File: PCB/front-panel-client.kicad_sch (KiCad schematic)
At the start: 7 parts, among them IC16 PMV20ENR, IC18 PMV20ENR, J10 67996-408HLF

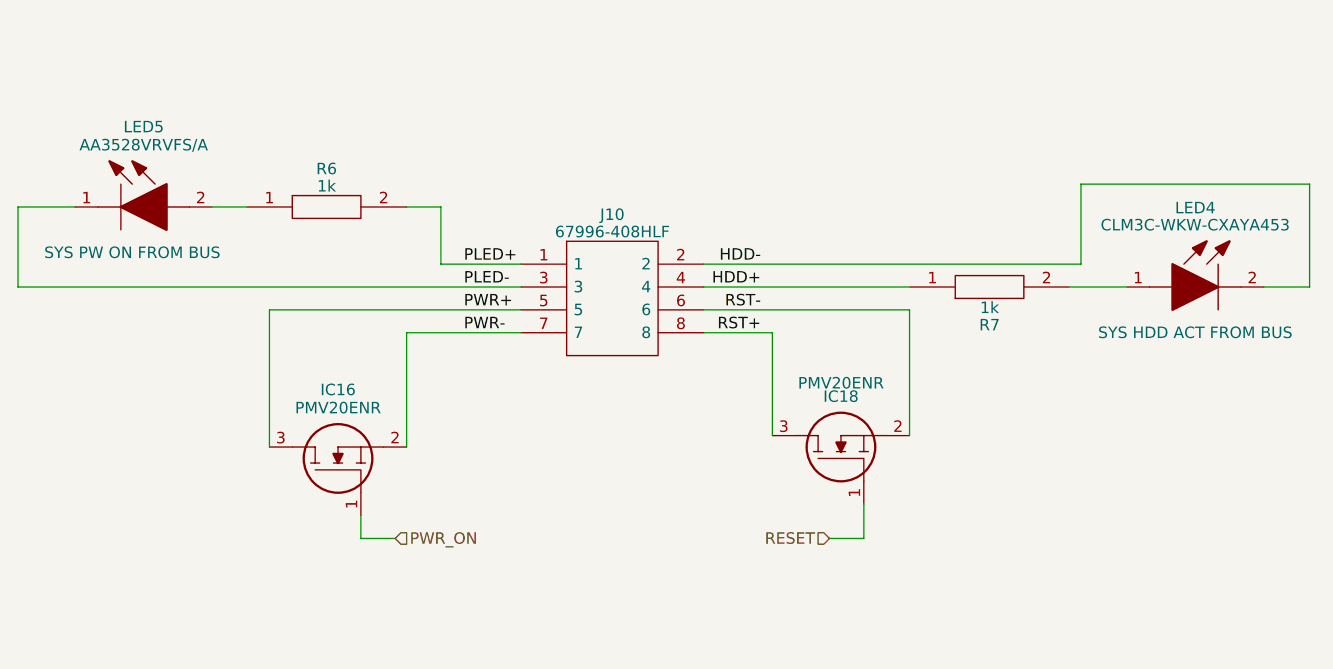
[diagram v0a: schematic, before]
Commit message: add pullup/down resistors and fix oro 6p lines with boot1/0
closes #24
closes #21
closes #15
closes #12
closes #6
closes #3
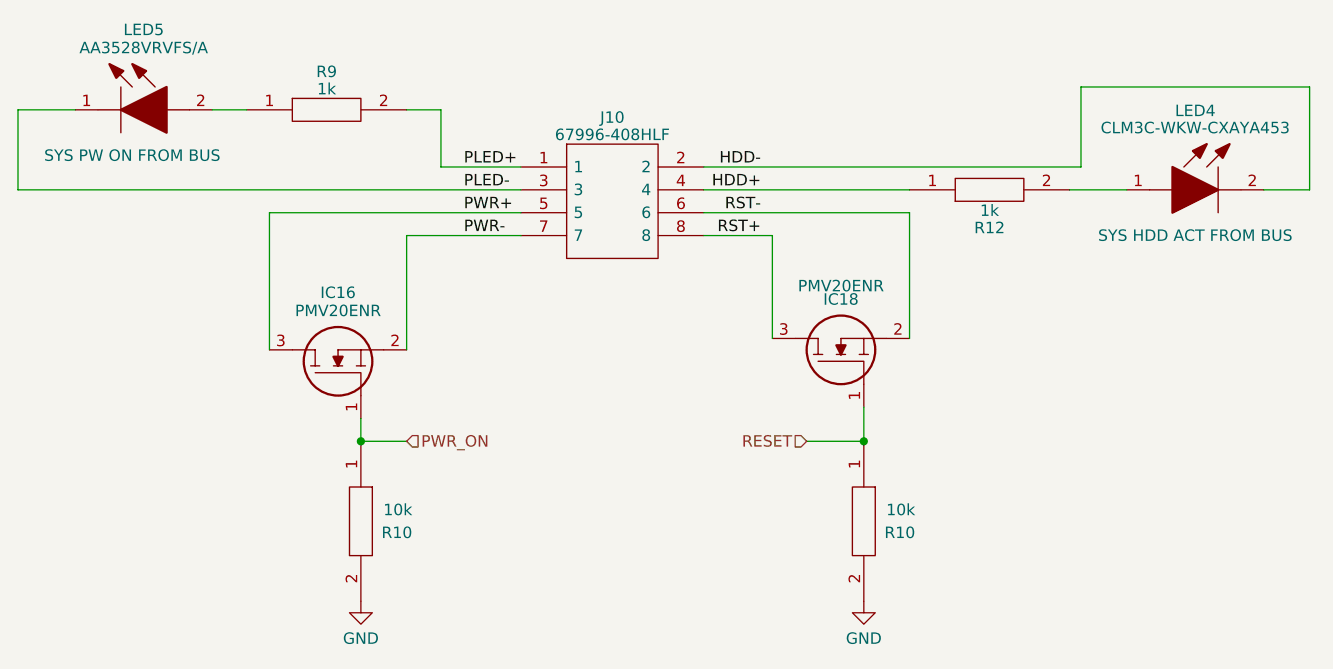
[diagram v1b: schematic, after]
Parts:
- added R10 (x2): 10k, SamacSys_Parts:RESC5025X65N, symbol SamacSys_Parts:RC2010JK-0710KL
- renumbered R7 to R12, R6 to R9
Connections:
- net PWR_ON: now also R10.1
- net RESET: now also R10.1
- new net GND: R10.2, R10.2
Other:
- moved on the sheet: IC16, IC18, J10, LED4, LED5, R12, R9

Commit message: switch 10k and 4.7k resistors to smaller packages (closes #32)
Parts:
- R10: footprint SamacSys_Parts:RESC5025X65N -> RESC5025X65N
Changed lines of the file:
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@@
       (effects (font (size 1.27 1.27)) (justify right))
     )
-    (property "Footprint" "SamacSys_Parts:RESC5025X65N" (at 173.99 134.62 0)
+    (property "Footprint" "RESC5025X65N" (at 173.99 134.62 0)
       (effects (font (size 1.27 1.27)) (justify left) hide)
     )
@@
       (effects (font (size 1.27 1.27)) (justify right))
     )
-    (property "Footprint" "SamacSys_Parts:RESC5025X65N" (at 118.11 134.62 0)
-      (effects (font (size 1.27 1.27)) (justify left) hide)
-    )
+    (property "Footprint" "RESC5025X65N" (at 118.11 134.62 0)
+      (effects (font (size 1.27 1.27)) (justify left) hide)
+    )

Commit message: actually reduce 10k package size (ref #32)
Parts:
- R10: footprint RESC5025X65N -> RESC1005X40N; symbol SamacSys_Parts:RC2010JK-0710KL -> SamacSys_Parts:RK73H1ETTP1002F; Arrow Part Number RC2010JK-0710KL -> RK73H1ETTP1002F; Arrow Price/Stock https://www.arrow.com/en/products/rc2010jk-0710kl/yageo -> https://www.arrow.com/en/products/rk73h1ettp1002f/koa-speer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; Height 0.65 -> 0.4; Manufacturer_Name KEMET -> KOA Speer; Manufacturer_Part_Number RC2010JK-0710KL -> RK73H1ETTP1002F; Mouser Part Number 603-RC2010JK-0710KL -> 660-RK73H1ETTP1002F; Mouser Price/Stock https://www.mouser.co.uk/ProductDetail/YAGEO/RC2010JK-0710K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 -> https://www.mouser.co.uk/ProductDetail/KOA-Speer/RK73H1ETTP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
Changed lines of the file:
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@@
     )
   )
-  (symbol (lib_id "SamacSys_Parts:RC2010JK-0710KL") (at 172.72 120.65 270) (unit 1)
+  (symbol (lib_id "SamacSys_Parts:RK73H1ETTP1002F") (at 172.72 120.65 270) (unit 1)
     (in_bom yes) (on_board yes) (dnp no)
     (property "Reference" "R10" (at 178.435 130.81 90)
@@
       (effects (font (size 1.27 1.27)) (justify right))
     )
-    (property "Footprint" "RESC5025X65N" (at 173.99 134.62 0)
-      (effects (font (size 1.27 1.27)) (justify left) hide)
-    )
-    (property "Datasheet" "https://www.arrow.com/en/products/rc2010jk-0710kl/yageo" (at 171.45 134.62 0)
-      (effects (font (size 1.27 1.27)) (justify left) hide)
-    )
-    (property "Description" "Res Thick Film 2010 10K Ohm 5% 0.75W(3/4W) +/-100ppm/C Pad SMD T/R" (at 168.91 134.62 0)
-      (effects (font (size 1.27 1.27)) (justify left) hide)
-    )
-    (property "Height" "0.65" (at 166.37 134.62 0)
-      (effects (font (size 1.27 1.27)) (justify left) hide)
-    )
-    (property "Manufacturer_Name" "KEMET" (at 163.83 134.62 0)
-      (effects (font (size 1.27 1.27)) (justify left) hide)
-    )
-    (property "Manufacturer_Part_Number" "RC2010JK-0710KL" (at 161.29 134.62 0)
-      (effects (font (size 1.27 1.27)) (justify left) hide)
-    )
-    (property "Mouser Part Number" "603-RC2010JK-0710KL" (at 158.75 134.62 0)
-      (effects (font (size 1.27 1.27)) (justify left) hide)
-    )
-    (property "Mouser Price/Stock" "https://www.mouser.co.uk/ProductDetail/YAGEO/RC2010JK-0710KL?qs=sNpmnPgvziOLj5uuquGIow%3D%3D" (at 156.21 134.62 0)
-      (effects (font (size 1.27 1.27)) (justify left) hide)
-    )
-    (property "Arrow Part Number" "RC2010JK-0710KL" (at 153.67 134.62 0)
-      (effects (font (size 1.27 1.27)) (justify left) hide)
-    )
-    (property "Arrow Price/Stock" "https://www.arrow.com/en/products/rc2010jk-0710kl/yageo" (at 151.13 134.62 0)
+    (property "Footprint" "RESC1005X40N" (at 173.99 134.62 0)
+      (effects (font (size 1.27 1.27)) (justify left) hide)
+    )
+    (property "Datasheet" "http://www.koaspeer.com/catimages/Products/RK73-RT/RK73-RT.pdf" (at 171.45 134.62 0)
+      (effects (font (size 1.27 1.27)) (justify left) hide)
+    )
+    (property "Description" "Resistor,ThickFilm1005,0.063W,10kohm" (at 168.91 134.62 0)
+      (effects (font (size 1.27 1.27)) (justify left) hide)
+    )
+    (property "Height" "0.4" (at 166.37 134.62 0)
+      (effects (font (size 1.27 1.27)) (justify left) hide)
+    )
+    (property "Manufacturer_Name" "KOA Speer" (at 163.83 134.62 0)
+      (effects (font (size 1.27 1.27)) (justify left) hide)
+    )
+    (property "Manufacturer_Part_Number" "RK73H1ETTP1002F" (at 161.29 134.62 0)
+      (effects (font (size 1.27 1.27)) (justify left) hide)
+    )
+    (property "Mouser Part Number" "660-RK73H1ETTP1002F" (at 158.75 134.62 0)
+      (effects (font (size 1.27 1.27)) (justify left) hide)
+    )
+    (property "Mouser Price/Stock" "https://www.mouser.co.uk/ProductDetail/KOA-Speer/RK73H1ETTP1002F?qs=uLfVlVfCHH2OZ4JTybrBPQ%3D%3D" (at 156.21 134.62 0)
+      (effects (font (size 1.27 1.27)) (justify left) hide)
+    )
+    (property "Arrow Part Number" "RK73H1ETTP1002F" (at 153.67 134.62 0)
+      (effects (font (size 1.27 1.27)) (justify left) hide)
+    )
+    (property "Arrow Price/Stock" "https://www.arrow.com/en/products/rk73h1ettp1002f/koa-speer-electronics?region=nac" (at 151.13 134.62 0)
       (effects (font (size 1.27 1.27)) (justify left) hide)
     )
@@
     )
   )
-  (symbol (lib_id "SamacSys_Parts:RC2010JK-0710KL") (at 116.84 120.65 270) (unit 1)
+  (symbol (lib_id "SamacSys_Parts:RK73H1ETTP1002F") (at 116.84 120.65 270) (unit 1)
     (in_bom yes) (on_board yes) (dnp no)
     (property "Reference" "R10" (at 122.555 130.81 90)
@@
       (effects (font (size 1.27 1.27)) (justify right))
     )
-    (property "Footprint" "RESC5025X65N" (at 118.11 134.62 0)
-      (effects (font (size 1.27 1.27)) (justify left) hide)
-    )
-    (property "Datasheet" "https://www.arrow.com/en/products/rc2010jk-0710kl/yageo" (at 115.57 134.62 0)
-      (effects (font (size 1.27 1.27)) (justify left) hide)
-    )
-    (property "Description" "Res Thick Film 2010 10K Ohm 5% 0.75W(3/4W) +/-100ppm/C Pad SMD T/R" (at 113.03 134.62 0)
-      (effects (font (size 1.27 1.27)) (justify left) hide)
-    )
-    (property "Height" "0.65" (at 110.49 134.62 0)
-      (effects (font (size 1.27 1.27)) (justify left) hide)
-    )
-    (property "Manufacturer_Name" "KEMET" (at 107.95 134.62 0)
-      (effects (font (size 1.27 1.27)) (justify left) hide)
-    )
-    (property "Manufacturer_Part_Number" "RC2010JK-0710KL" (at 105.41 134.62 0)
-      (effects (font (size 1.27 1.27)) (justify left) hide)
-    )
-    (property "Mouser Part Number" "603-RC2010JK-0710KL" (at 102.87 134.62 0)
-      (effects (font (size 1.27 1.27)) (justify left) hide)
-    )
-    (property "Mouser Price/Stock" "https://www.mouser.co.uk/ProductDetail/YAGEO/RC2010JK-0710KL?qs=sNpmnPgvziOLj5uuquGIow%3D%3D" (at 100.33 134.62 0)
-      (effects (font (size 1.27 1.27)) (justify left) hide)
-    )
-    (property "Arrow Part Number" "RC2010JK-0710KL" (at 97.79 134.62 0)
-      (effects (font (size 1.27 1.27)) (justify left) hide)
-    )
-    (property "Arrow Price/Stock" "https://www.arrow.com/en/products/rc2010jk-0710kl/yageo" (at 95.25 134.62 0)
-      (effects (font (size 1.27 1.27)) (justify left) hide)
-    )
+    (property "Footprint" "RESC1005X40N" (at 118.11 134.62 0)
+      (effects (font (size 1.27 1.27)) (justify left) hide)
+    )
+    (property "Datasheet" "http://www.koaspeer.com/catimages/Products/RK73-RT/RK73-RT.pdf" (at 115.57 134.62 0)
+      (effects (font (size 1.27 1.27)) (justify left) hide)
+    )
+    (property "Description" "Resistor,ThickFilm1005,0.063W,10kohm" (at 113.03 134.62 0)
+      (effects (font (size 1.27 1.27)) (justify left) hide)
+    )
+    (property "Height" "0.4" (at 110.49 134.62 0)
+      (effects (font (size 1.27 1.27)) (justify left) hide)
+    )
+    (property "Manufacturer_Name" "KOA Speer" (at 107.95 134.62 0)
+      (effects (font (size 1.27 1.27)) (justify left) hide)
+    )
+    (property "Manufacturer_Part_Number" "RK73H1ETTP1002F" (at 105.41 134.62 0)
+      (effects (font (size 1.27 1.27)) (justify left) hide)
+    )
+    (property "Mouser Part Number" "660-RK73H1ETTP1002F" (at 102.87 134.62 0)
+      (effects (font (size 1.27 1.27)) (justify left) hide)
+    )
+    (property "Mouser Price/Stock" "https://www.mouser.co.uk/ProductDetail/KOA-Speer/RK73H1ETTP1002F?qs=uLfVlVfCHH2OZ4JTybrBPQ%3D%3D" (at 100.33 134.62 0)
+      (effects (font (size 1.27 1.27)) (justify left) hide)
+    )
+    (property "Arrow Part Number" "RK73H1ETTP1002F" (at 97.79 134.62 0)
+      (effects (font (size 1.27 1.27)) (justify left) hide)
+    )
+    (property "Arrow Price/Stock" "https://www.arrow.com/en/products/rk73h1ettp1002f/koa-speer-electronics?region=nac" (at 95.25 134.62 0)
+      (effects (font (size 1.27 1.27)) (justify left) hide)
+    )

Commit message: re-annotate schematic
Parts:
- renumbered R9 to R10, R12 to R13
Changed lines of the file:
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@@
   (symbol (lib_id "SamacSys_Parts:SG73P2ATTD102J") (at 177.8 92.71 0) (mirror x) (unit 1)
     (in_bom yes) (on_board yes) (dnp no) (fields_autoplaced)
-    (property "Reference" "R12" (at 186.69 96.9391 0)
+    (property "Reference" "R13" (at 186.69 96.9391 0)
       (effects (font (size 1.27 1.27)))
     )
@@
       (project "OroLink"
         (path "/e89dcd22-1250-4a5b-b778-1c95a0dd623d/6eeb4496-d532-42b5-95b8-3d397c9a21d1"
-          (reference "R12") (unit 1)
+          (reference "R13") (unit 1)
         )
       )
@@
         )
         (path "/e89dcd22-1250-4a5b-b778-1c95a0dd623d/6eeb4496-d532-42b5-95b8-3d397c9a21d1"
-          (reference "R11") (unit 1)
+          (reference "R12") (unit 1)
         )
       )
@@
         )
         (path "/e89dcd22-1250-4a5b-b778-1c95a0dd623d/6eeb4496-d532-42b5-95b8-3d397c9a21d1"
-          (reference "R10") (unit 1)
+          (reference "R11") (unit 1)
         )
       )
@@
   (symbol (lib_id "SamacSys_Parts:SG73P2ATTD102J") (at 104.14 83.82 0) (unit 1)
     (in_bom yes) (on_board yes) (dnp no) (fields_autoplaced)
-    (property "Reference" "R9" (at 113.03 79.5909 0)
+    (property "Reference" "R10" (at 113.03 79.5909 0)
       (effects (font (size 1.27 1.27)))
     )
@@
       (project "OroLink"
         (path "/e89dcd22-1250-4a5b-b778-1c95a0dd623d/6eeb4496-d532-42b5-95b8-3d397c9a21d1"
-          (reference "R9") (unit 1)
-        )
-      )
+          (reference "R10") (unit 1)
+        )
+      )

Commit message: switch out linear regular for one with larger max current (closes #43)
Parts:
- renumbered R10 to R11, R13 to R14
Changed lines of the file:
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@@
   (symbol (lib_id "power:GND") (at 116.84 138.43 0) (unit 1)
     (in_bom yes) (on_board yes) (dnp no) (fields_autoplaced)
-    (property "Reference" "#PWR026" (at 116.84 144.78 0)
+    (property "Reference" "#PWR027" (at 116.84 144.78 0)
       (effects (font (size 1.27 1.27)) hide)
     )
@@
       (project "OroLink"
         (path "/e89dcd22-1250-4a5b-b778-1c95a0dd623d/6eeb4496-d532-42b5-95b8-3d397c9a21d1"
-          (reference "#PWR026") (unit 1)
+          (reference "#PWR027") (unit 1)
         )
       )
@@
   (symbol (lib_id "SamacSys_Parts:SG73P2ATTD102J") (at 177.8 92.71 0) (mirror x) (unit 1)
     (in_bom yes) (on_board yes) (dnp no) (fields_autoplaced)
-    (property "Reference" "R13" (at 186.69 96.9391 0)
+    (property "Reference" "R14" (at 186.69 96.9391 0)
       (effects (font (size 1.27 1.27)))
     )
@@
       (project "OroLink"
         (path "/e89dcd22-1250-4a5b-b778-1c95a0dd623d/6eeb4496-d532-42b5-95b8-3d397c9a21d1"
-          (reference "R13") (unit 1)
+          (reference "R14") (unit 1)
         )
       )
@@
         )
         (path "/e89dcd22-1250-4a5b-b778-1c95a0dd623d/6eeb4496-d532-42b5-95b8-3d397c9a21d1"
-          (reference "R12") (unit 1)
+          (reference "R13") (unit 1)
         )
       )
@@
         )
         (path "/e89dcd22-1250-4a5b-b778-1c95a0dd623d/6eeb4496-d532-42b5-95b8-3d397c9a21d1"
-          (reference "R11") (unit 1)
+          (reference "R12") (unit 1)
         )
       )
@@
   (symbol (lib_id "SamacSys_Parts:SG73P2ATTD102J") (at 104.14 83.82 0) (unit 1)
     (in_bom yes) (on_board yes) (dnp no) (fields_autoplaced)
-    (property "Reference" "R10" (at 113.03 79.5909 0)
+    (property "Reference" "R11" (at 113.03 79.5909 0)
       (effects (font (size 1.27 1.27)))
     )
@@
       (project "OroLink"
         (path "/e89dcd22-1250-4a5b-b778-1c95a0dd623d/6eeb4496-d532-42b5-95b8-3d397c9a21d1"
-          (reference "R10") (unit 1)
+          (reference "R11") (unit 1)
         )
       )
@@
   (symbol (lib_id "power:GND") (at 172.72 138.43 0) (unit 1)
     (in_bom yes) (on_board yes) (dnp no) (fields_autoplaced)
-    (property "Reference" "#PWR027" (at 172.72 144.78 0)
+    (property "Reference" "#PWR028" (at 172.72 144.78 0)
       (effects (font (size 1.27 1.27)) hide)
     )
@@
       (project "OroLink"
         (path "/e89dcd22-1250-4a5b-b778-1c95a0dd623d/6eeb4496-d532-42b5-95b8-3d397c9a21d1"
-          (reference "#PWR027") (unit 1)
-        )
-      )
+          (reference "#PWR028") (unit 1)
+        )
+      )

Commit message: initial rev6
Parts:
- renumbered R11 to R10, R14 to R13
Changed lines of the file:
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@@
   (title_block
     (title "Oro Link")
-    (date "2023-06-02")
-    (rev "5")
+    (date "2023-07-02")
+    (rev "6")
     (company "Oro Operating System")
     (comment 1 "://oro.sh")
@@
   (symbol (lib_id "power:GND") (at 116.84 138.43 0) (unit 1)
     (in_bom yes) (on_board yes) (dnp no) (fields_autoplaced)
-    (property "Reference" "#PWR027" (at 116.84 144.78 0)
+    (property "Reference" "#PWR026" (at 116.84 144.78 0)
       (effects (font (size 1.27 1.27)) hide)
     )
@@
       (project "OroLink"
         (path "/e89dcd22-1250-4a5b-b778-1c95a0dd623d/6eeb4496-d532-42b5-95b8-3d397c9a21d1"
-          (reference "#PWR027") (unit 1)
+          (reference "#PWR026") (unit 1)
         )
       )
@@
   (symbol (lib_id "SamacSys_Parts:SG73P2ATTD102J") (at 177.8 92.71 0) (mirror x) (unit 1)
     (in_bom yes) (on_board yes) (dnp no) (fields_autoplaced)
-    (property "Reference" "R14" (at 186.69 96.9391 0)
+    (property "Reference" "R13" (at 186.69 96.9391 0)
       (effects (font (size 1.27 1.27)))
     )
@@
       (project "OroLink"
         (path "/e89dcd22-1250-4a5b-b778-1c95a0dd623d/6eeb4496-d532-42b5-95b8-3d397c9a21d1"
-          (reference "R14") (unit 1)
+          (reference "R13") (unit 1)
         )
       )
@@
         )
         (path "/e89dcd22-1250-4a5b-b778-1c95a0dd623d/6eeb4496-d532-42b5-95b8-3d397c9a21d1"
-          (reference "R13") (unit 1)
+          (reference "R12") (unit 1)
         )
       )
@@
         )
         (path "/e89dcd22-1250-4a5b-b778-1c95a0dd623d/6eeb4496-d532-42b5-95b8-3d397c9a21d1"
-          (reference "R12") (unit 1)
+          (reference "R11") (unit 1)
         )
       )
@@
   (symbol (lib_id "SamacSys_Parts:SG73P2ATTD102J") (at 104.14 83.82 0) (unit 1)
     (in_bom yes) (on_board yes) (dnp no) (fields_autoplaced)
-    (property "Reference" "R11" (at 113.03 79.5909 0)
+    (property "Reference" "R10" (at 113.03 79.5909 0)
       (effects (font (size 1.27 1.27)))
     )
@@
       (project "OroLink"
         (path "/e89dcd22-1250-4a5b-b778-1c95a0dd623d/6eeb4496-d532-42b5-95b8-3d397c9a21d1"
-          (reference "R11") (unit 1)
+          (reference "R10") (unit 1)
         )
       )
@@
   (symbol (lib_id "power:GND") (at 172.72 138.43 0) (unit 1)
     (in_bom yes) (on_board yes) (dnp no) (fields_autoplaced)
-    (property "Reference" "#PWR028" (at 172.72 144.78 0)
+    (property "Reference" "#PWR027" (at 172.72 144.78 0)
       (effects (font (size 1.27 1.27)) hide)
     )
@@
       (project "OroLink"
         (path "/e89dcd22-1250-4a5b-b778-1c95a0dd623d/6eeb4496-d532-42b5-95b8-3d397c9a21d1"
-          (reference "#PWR028") (unit 1)
-        )
-      )
+          (reference "#PWR027") (unit 1)
+        )
+      )
